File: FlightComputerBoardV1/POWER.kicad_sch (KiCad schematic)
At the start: 44 parts, among them U14 TPS56A37RPAR, U7 TPS56A37RPAR

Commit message: temp and power sensor
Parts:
- added C47, C48, C49: 0.1uF, symbol Device:C
- added C50, C51: 100nF, symbol Device:C
- added U15: LM74700, Package_TO_SOT_SMD:SOT-23-6, symbol Power_Management:LM74700
- added U16: INA260, Package_SO:TSSOP-16_4.4x5mm_P0.65mm, symbol Sensor_Energy:INA260
- added U17: MCP9808_DFN, Package_DFN_QFN:DFN-8-1EP_3x2mm_P0.5mm_EP1.7x1.4mm, symbol Sensor_Temperature:MCP9808_DFN
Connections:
- net +24V: now also C49.1, U15.4 (CATHODE), U16.1 (IN+), U16.12 (VBUS), U16.2 (IN+), U16.3 (IN+)
- new net: C48.2, U15.1 (VCAP)
- new net +3V3: C50.1, C51.1, U16.10 (VS), U17.8 (V_{DD})
- new net Battery: C47.1, C48.1, U15.3 (EN), U15.6 (ANODE)
- new net GND: C47.2, C49.2, C50.2, C51.2, U15.2 (GND), U16.11 (GND), U16.4 (A1), U16.5 (A0), U16.6 (GND), U17.4 (GND), U17.5 (A2), U17.6 (A1), U17.7 (A0), U17.9 (EP/GND)
- new net I2C0_SCL: U16.9 (SCL), U17.2 (SCL)
- new net I2C0_SDA: U16.8 (SDA), U17.1 (SDA)
- new net LOAD_POWER_IN: U16.14 (IN-), U16.15 (IN-), U16.16 (IN-)
- no-connect marks 0 -> 2

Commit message: diode mosfet selection
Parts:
- added C52, C53, C54: 0.1uF, symbol Device:C
- added MOSFET1, MOSFET2: NVMFS6H848NLT1G, DFN6_5X6_SO8FL_488AA_ONS, symbol NVMFS6H848NLT1G:NVMFS6H848NLT1G
- added U18: LM74700, Package_TO_SOT_SMD:SOT-23-6, symbol Power_Management:LM74700
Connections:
- net +24V: no longer C49.1, U15.4 (CATHODE)
- net Battery: now also C52.1, C53.1, MOSFET2.1, MOSFET2.2, MOSFET2.3, U18.3 (EN), U18.6 (ANODE); no longer C47.1, C48.1, U15.3 (EN), U15.6 (ANODE)
- net GND: now also C52.2, C54.2, U18.2 (GND)
- net at U15.5 (GATE): now also MOSFET1.4
- new net: MOSFET2.4, U18.5 (GATE)
- new net: C53.2, U18.1 (VCAP)
- new net Output: C49.1, C54.1, MOSFET1.5, MOSFET1.6, MOSFET2.5, MOSFET2.6, U15.4 (CATHODE), U18.4 (CATHODE)
- new net Power Supply: C47.1, C48.1, MOSFET1.1, MOSFET1.2, MOSFET1.3, U15.3 (EN), U15.6 (ANODE)
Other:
- moved on the sheet: C10, C11, C12, C13, C14, C15, C16, C17, C18, C19, C20, C36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

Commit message: more power
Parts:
- added CR1, CR2: SMBJ26A, SMBJSeries_LTF, symbol SMBJ26A:SMBJ26A
- C47, C52: value 0.1uF -> 22nF
- C49, C54: value 0.1uF -> 47uF
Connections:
- net Battery: now also CR1.1
- net GND: now also CR1.2, CR2.2
- net Power Supply: now also CR2.1
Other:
- moved on the sheet: C47, C52

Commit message: Addition to MCU sheet and peripheral connection complete
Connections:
- net I2C0_SCL renamed SCL_I2C_1
- net I2C0_SDA renamed SDA_I2C_1
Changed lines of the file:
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@@
 		)
 	)
-	(hierarchical_label "I2C0_SDA"
+	(hierarchical_label "SCL_I2C_1"
+		(shape bidirectional)
+		(at 233.68 243.84 0)
+		(effects
+			(font
+				(size 1.27 1.27)
+			)
+			(justify left)
+		)
+	)
+	(hierarchical_label "SDA_I2C_1"
+		(shape bidirectional)
+		(at 273.05 238.76 180)
+		(effects
+			(font
+				(size 1.27 1.27)
+			)
+			(justify right)
+		)
+	)
+	(hierarchical_label "SDA_I2C_1"
 		(shape bidirectional)
 		(at 233.68 246.38 0)
@@
 		)
 	)
-	(hierarchical_label "I2C0_SCL"
-		(shape bidirectional)
-		(at 233.68 243.84 0)
-		(effects
-			(font
-				(size 1.27 1.27)
-			)
-			(justify left)
-		)
-	)
-	(hierarchical_label "I2C0_SCL"
+	(hierarchical_label "SCL_I2C_1"
 		(shape bidirectional)
 		(at 273.05 241.3 180)
 		(effects
 			(font
-				(size 1.27 1.27)
-			)
-			(justify right)
-		)
-	)
-	(hierarchical_label "I2C0_SDA"
-		(shape bidirectional)
-		(at 273.05 238.76 180)
-		(effects
-			(font

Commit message: more buck
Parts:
- added U21: PTPS2116DRLR, DRL0008A-MFG, symbol PTPS2116DRLR:PTPS2116DRLR
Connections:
- net +5V renamed +5V_Buck
- net +5V_Buck: now also U21.3 (VIN1)
- new net +5V_USB: U21.6 (VIN2)
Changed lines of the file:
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@@
 	(rectangle
 		(start 46.99 69.85)
-		(end 261.62 194.31)
+		(end 447.04 194.31)
 		(stroke
 			(width 0.508)
@@
 	(wire
 		(pts
+			(xy 300.99 90.17) (xy 311.15 90.17)
+		)
+		(stroke
+			(width 0)
+			(type default)
+		)
+	)
+	(wire
+		(pts
 			(xy 186.69 99.06) (xy 186.69 101.6)
 		)
@@
 	(wire
 		(pts
+			(xy 299.72 92.71) (xy 300.99 92.71)
+		)
+		(stroke
+			(width 0)
+			(type default)
+		)
+	)
+	(wire
+		(pts
 			(xy 99.06 172.72) (xy 99.06 184.15)
 		)
@@
 	(wire
 		(pts
+			(xy 299.72 87.63) (xy 311.15 87.63)
+		)
+		(stroke
+			(width 0)
+			(type default)
+		)
+	)
+	(wire
+		(pts
 			(xy 99.06 95.25) (xy 99.06 100.33)
 		)
@@
 	(wire
 		(pts
+			(xy 300.99 92.71) (xy 300.99 90.17)
+		)
+		(stroke
+			(width 0)
+			(type default)
+		)
+	)
+	(wire
+		(pts
 			(xy 72.39 327.66) (xy 72.39 330.2)
 		)
@@
 		)
 	)
-	(global_label "+5V"
+	(global_label "+5V_Buck"
 		(shape input)
 		(at 250.19 86.36 0)
@@
 		)
 		(property "Intersheetrefs" "${INTERSHEET_REFS}"
-			(at 257.0457 86.36 0)
+			(at 262.549 86.36 0)
 			(hide yes)
 			(show_name no)
@@
 		)
 	)
+	(global_label "+5V_USB"
+		(shape input)
+		(at 299.72 92.71 180)
+		(fields_autoplaced yes)
+		(effects
+			(font
+				(size 1.27 1.27)
+			)
+			(justify right)
+		)
+		(property "Intersheetrefs" "${INTERSHEET_REFS}"
+			(at 288.0867 92.71 0)
+			(hide yes)
+			(show_name no)
+			(do_not_autoplace no)
+			(effects
+				(font
+					(size 1.27 1.27)
+				)
+				(justify right)
+			)
+		)
+	)
+	(global_label "+5V_Buck"
+		(shape input)
+		(at 299.72 87.63 180)
+		(fields_autoplaced yes)
+		(effects
+			(font
+				(size 1.27 1.27)
+			)
+			(justify right)
+		)
+		(property "Intersheetrefs" "${INTERSHEET_REFS}"
+			(at 287.361 87.63 0)
+			(hide yes)
+			(show_name no)
+			(do_not_autoplace no)
+			(effects
+				(font
+					(size 1.27 1.27)
+				)
+				(justify right)
+			)
+		)
+	)
 	(hierarchical_label "SCL_I2C_1"
 		(shape bidirectional)
@@
 					(unit 1)
 				)
+			)
+		)
+	)
+	(symbol
+		(lib_id "PTPS2116DRLR:PTPS2116DRLR")
+		(at 311.15 87.63 0)
+		(unit 1)
+		(body_style 1)
+		(exclude_from_sim no)
+		(in_bom yes)
+		(on_board yes)
+		(in_pos_files yes)
+		(dnp no)
+		(fields_autoplaced yes)
+		(property "Reference" "U21"
+			(at 330.2 77.47 0)
+			(show_name no)
+			(do_not_autoplace no)
+			(effects
+				(font
+					(size 1.524 1.524)
+				)
+			)
+		)
+		(property "Value" "PTPS2116DRLR"
+			(at 330.2 80.01 0)
+			(show_name no)
+			(do_not_autoplace no)
+			(effects
+				(font
+					(size 1.524 1.524)
+				)
+			)
+		)
+		(property "Footprint" "DRL0008A-MFG"
+			(at 311.15 87.63 0)
+			(hide yes)
+			(show_name no)
+			(do_not_autoplace no)
+			(effects
+				(font
+					(size 1.27 1.27)
+					(italic yes)
+				)
+			)
+		)
+		(property "Datasheet" "https://www.ti.com/lit/gpn/tps2116"
+			(at 311.15 87.63 0)
+			(hide yes)
+			(show_name no)
+			(do_not_autoplace no)
+			(effects
+				(font
+					(size 1.27 1.27)
+					(italic yes)
+				)
+			)
+		)
+		(property "Description" ""
+			(at 311.15 87.63 0)
+			(hide yes)
+			(show_name no)
+			(do_not_autoplace no)
+			(effects
+				(font
+					(size 1.27 1.27)
+				)
+			)
+		)
+		(pin "3"
+		)
+		(pin "8"
+		)
+		(pin "4"
+		)
+		(pin "7"
+		)
+		(pin "1"
+		)
+		(pin "6"
+		)
+		(pin "2"
+		)
+		(pin "5"
+		)
+		(instances
+			(project "FlightComputerBoardV1"
+				(path "/7795ce7a-d456-4fa5-b86a-75a229c2d679/3649f41a-e3eb-4228-8a3a-5b23b97352ea"
+					(reference "U21")
+					(unit 1)
+				)

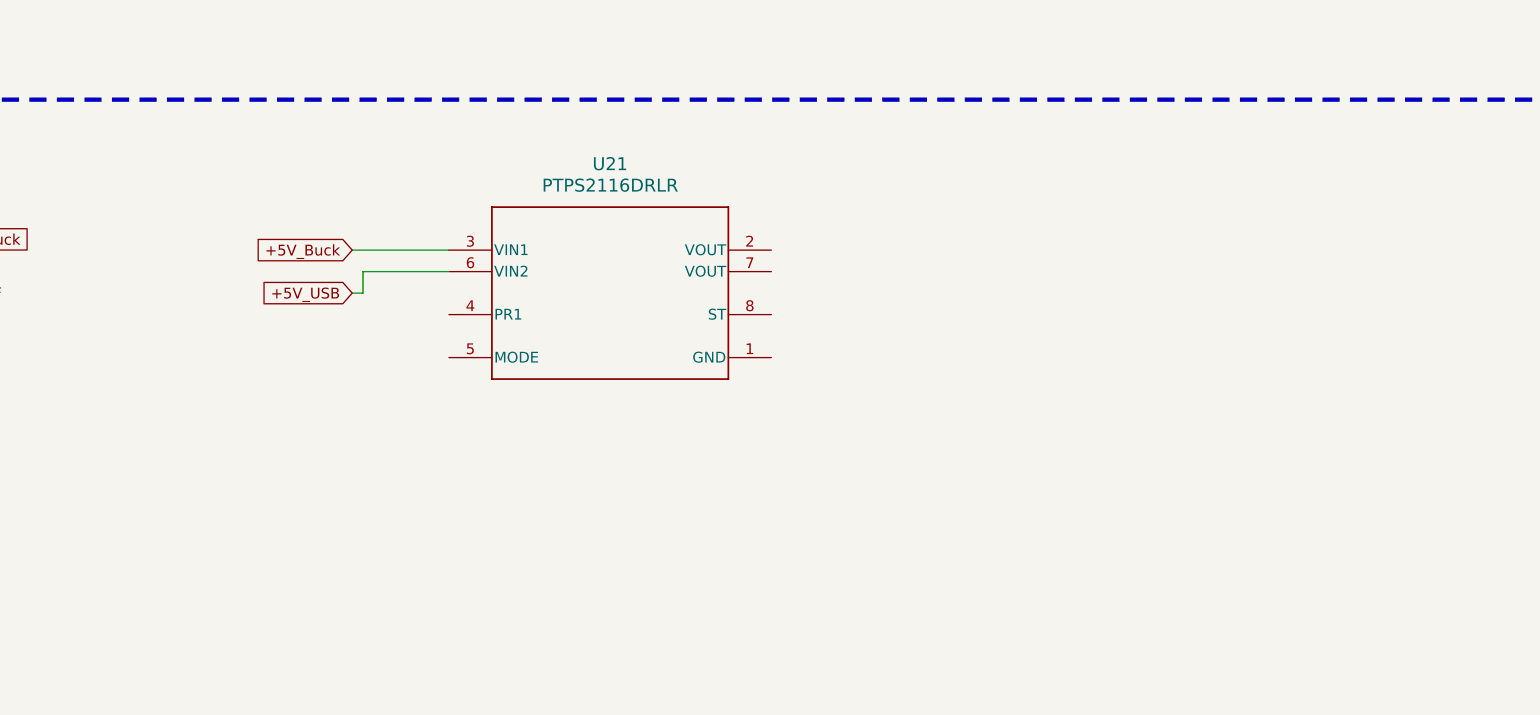
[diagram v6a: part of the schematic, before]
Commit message: priority power mux switching
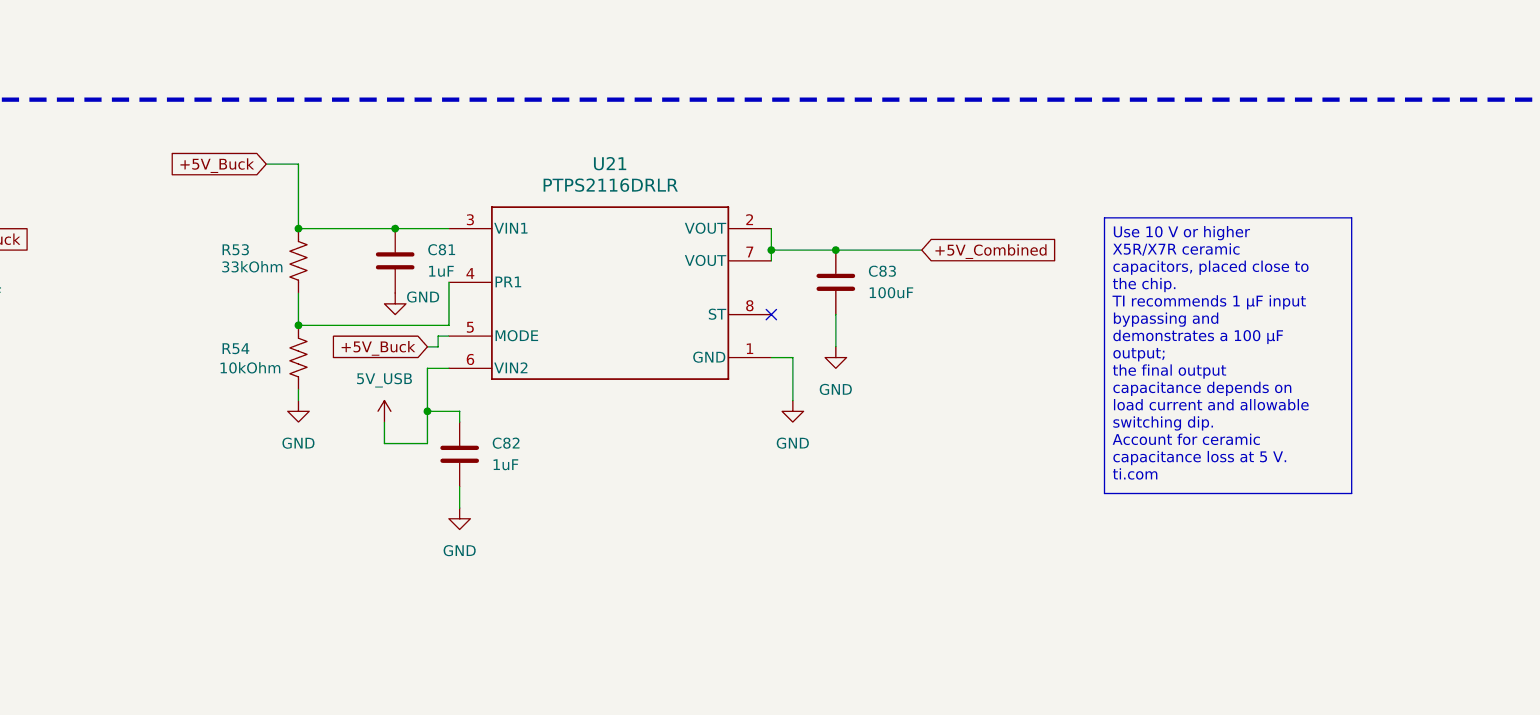
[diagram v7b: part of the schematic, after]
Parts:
- added C81, C82: 1uF, symbol Device:C
- added C83: 100uF, symbol Device:C
- added R53: 33kOhm, symbol Device:R_US
- added R54: 10kOhm, symbol Device:R_US
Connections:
- net +5V_Buck: now also U21.5 (MODE), C81.1, R53.1
- net GND: now also U21.1 (GND), C81.2, C82.2, C83.2, R54.2
- net +5V_Combined: now reaches U21.2 (VOUT)
- net +5V_Combined: now also U21.7 (VOUT), C83.1
- net at U21.4 (PR1): now also R53.2, R54.1
- net +5V_USB renamed 5V_USB
- net 5V_USB: now also C82.1
- no-connect marks 2 -> 3

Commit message: added ldo and fixed power mux
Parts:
- added C84, C85: 1uF, DBV0005A_N, symbol Device:C
- added U22: TLV75533PDBVR, DBV0005A_N, symbol TLV75533PDBVR:TLV75533PDBVR
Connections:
- net +5V_Buck: no longer C81.1, R53.1, U21.3 (VIN1), U21.5 (MODE)
- net 5V_USB: now also C84.1, U22.1 (IN), U22.3 (EN); no longer C82.1, U21.6 (VIN2)
- net GND: now also C84.2, C85.2, U22.2 (GND)
- net +3.3V renamed +3.3V_Buck
- net +3.3V_Buck: now also C81.1, R53.1, U21.3 (VIN1), U21.5 (MODE)
- net +5V_Combined renamed +3V
- new net +3V3_USB: C85.1, U22.5 (OUT)
- new net 3V3_USB: C82.1, U21.6 (VIN2)
- no-connect marks 3 -> 4
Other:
- moved on the sheet: C81, C82, C83, R53, R54, U21
